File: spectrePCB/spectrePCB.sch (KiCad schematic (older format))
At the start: 23 parts, among them J1 USB_C_Receptacle, SW1 SW_Push, U1 Opamp_Dual_Generic, U2 ADG633YRU, U3 ATmega32U4-AU, U4 ADG633YRU, Y1 16MHz

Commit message: added footprints to components
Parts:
- C1, C2, C3, C4, C5, C6, C7: footprint (none) -> Capacitor_SMD:C_0603_1608Metric
- D1: footprint (none) -> LED_SMD:LED_0603_1608Metric
- F1: footprint (none) -> Fuse:Fuse_0603_1608Metric
- J1: footprint (none) -> Connector_USB:USB_C_Receptacle_Amphenol_12401548E4-2A
- R1, R2, R3, R4, R5, R6, R7: footprint (none) -> Resistor_SMD:R_0201_0603Metric
- SW1: footprint (none) -> Button_Switch_SMD:SW_SPST_TL3305A
- U1: footprint (none) -> Package_SO:SOIC-8_3.9x4.9mm_P1.27mm
- Y1: footprint (none) -> Crystal:Crystal_SMD_3225-4Pin_3.2x2.5mm
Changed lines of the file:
@@
 F 0 "R7" V 7150 4600 50  0000 C CNN
 F 1 "10k" V 7300 4600 50  0000 C CNN
-F 2 "" H 7250 4600 50  0001 C CNN
+F 2 "Resistor_SMD:R_0201_0603Metric" H 7250 4600 50  0001 C CNN
 F 3 "~" H 7250 4600 50  0001 C CNN
 	1    7250 4600
@@
 F 0 "R2" V 4495 3500 50  0000 C CNN
 F 1 "22" V 4586 3500 50  0000 C CNN
-F 2 "" H 4700 3500 50  0001 C CNN
+F 2 "Resistor_SMD:R_0201_0603Metric" H 4700 3500 50  0001 C CNN
 F 3 "~" H 4700 3500 50  0001 C CNN
 	1    4700 3500
@@
 F 0 "R4" V 4550 3600 50  0000 C CNN
 F 1 "22" V 4650 3600 50  0000 C CNN
-F 2 "" H 4450 3600 50  0001 C CNN
+F 2 "Resistor_SMD:R_0201_0603Metric" H 4450 3600 50  0001 C CNN
 F 3 "~" H 4450 3600 50  0001 C CNN
 	1    4450 3600
@@
 F 0 "C7" H 4842 4096 50  0000 L CNN
 F 1 "1uF" H 4842 4005 50  0000 L CNN
-F 2 "" H 4750 4050 50  0001 C CNN
+F 2 "Capacitor_SMD:C_0603_1608Metric" H 4750 4050 50  0001 C CNN
 F 3 "~" H 4750 4050 50  0001 C CNN
 	1    4750 4050
@@
 F 0 "C2" H 2142 1846 50  0000 L CNN
 F 1 "0.1uF" H 2142 1755 50  0000 L CNN
-F 2 "" H 2050 1800 50  0001 C CNN
+F 2 "Capacitor_SMD:C_0603_1608Metric" H 2050 1800 50  0001 C CNN
 F 3 "~" H 2050 1800 50  0001 C CNN
 	1    2050 1800
@@
 F 0 "C1" H 1742 1846 50  0000 L CNN
 F 1 "0.1uF" H 1742 1755 50  0000 L CNN
-F 2 "" H 1650 1800 50  0001 C CNN
+F 2 "Capacitor_SMD:C_0603_1608Metric" H 1650 1800 50  0001 C CNN
 F 3 "~" H 1650 1800 50  0001 C CNN
 	1    1650 1800
@@
 F 0 "C3" H 2542 1846 50  0000 L CNN
 F 1 "0.1uF" H 2542 1755 50  0000 L CNN
-F 2 "" H 2450 1800 50  0001 C CNN
+F 2 "Capacitor_SMD:C_0603_1608Metric" H 2450 1800 50  0001 C CNN
 F 3 "~" H 2450 1800 50  0001 C CNN
 	1    2450 1800
@@
 F 0 "C4" H 2892 1846 50  0000 L CNN
 F 1 "10uF" H 2892 1755 50  0000 L CNN
-F 2 "" H 2800 1800 50  0001 C CNN
+F 2 "Capacitor_SMD:C_0603_1608Metric" H 2800 1800 50  0001 C CNN
 F 3 "~" H 2800 1800 50  0001 C CNN
 	1    2800 1800
@@
 F 0 "C6" V 4500 2900 50  0000 C CNN
 F 1 "22pF" V 4600 2900 50  0000 C CNN
-F 2 "" H 4400 2900 50  0001 C CNN
+F 2 "Capacitor_SMD:C_0603_1608Metric" H 4400 2900 50  0001 C CNN
 F 3 "~" H 4400 2900 50  0001 C CNN
 	1    4400 2900
@@
 F 0 "C5" V 4200 2700 50  0000 C CNN
 F 1 "22pF" V 4300 2700 50  0000 C CNN
-F 2 "" H 4400 2700 50  0001 C CNN
+F 2 "Capacitor_SMD:C_0603_1608Metric" H 4400 2700 50  0001 C CNN
 F 3 "~" H 4400 2700 50  0001 C CNN
 	1    4400 2700
@@
 F 0 "Y1" V 4654 2944 50  0000 L CNN
 F 1 "16MHz" V 4745 2944 50  0000 L CNN
-F 2 "" H 4700 2800 50  0001 C CNN
+F 2 "Crystal:Crystal_SMD_3225-4Pin_3.2x2.5mm" H 4700 2800 50  0001 C CNN
 F 3 "~" H 4700 2800 50  0001 C CNN
 	1    4700 2800
@@
 F 0 "SW1" H 5000 2700 50  0000 C CNN
 F 1 "SW_Push" H 5000 2694 50  0001 C CNN
-F 2 "" H 5000 2700 50  0001 C CNN
+F 2 "Button_Switch_SMD:SW_SPST_TL3305A" H 5000 2700 50  0001 C CNN
 F 3 "~" H 5000 2700 50  0001 C CNN
 	1    5000 2500
@@
 F 0 "R1" H 5318 2146 50  0000 L CNN
 F 1 "10k" H 5318 2055 50  0000 L CNN
-F 2 "" H 5250 2100 50  0001 C CNN
+F 2 "Resistor_SMD:R_0201_0603Metric" H 5250 2100 50  0001 C CNN
 F 3 "~" H 5250 2100 50  0001 C CNN
 	1    5250 2100
@@
 F 0 "R6" H 2750 4200 50  0000 C CNN
 F 1 "5k" H 2750 4300 50  0000 C CNN
-F 2 "" H 2900 4250 50  0001 C CNN
+F 2 "Resistor_SMD:R_0201_0603Metric" H 2900 4250 50  0001 C CNN
 F 3 "~" H 2900 4250 50  0001 C CNN
 	1    2900 4250
@@
 F 0 "R5" H 2800 4200 50  0000 R CNN
 F 1 "5k" H 2800 4300 50  0000 R CNN
-F 2 "" H 2650 4250 50  0001 C CNN
+F 2 "Resistor_SMD:R_0201_0603Metric" H 2650 4250 50  0001 C CNN
 F 3 "~" H 2650 4250 50  0001 C CNN
 	1    2650 4250
@@
 F 0 "F1" V 2100 3000 50  0000 C CNN
 F 1 "500mA" V 2200 3000 50  0000 C CNN
-F 2 "" H 2200 2800 50  0001 L CNN
+F 2 "Fuse:Fuse_0603_1608Metric" H 2200 2800 50  0001 L CNN
 F 3 "~" H 2150 3000 50  0001 C CNN
 	1    2150 3000
@@
 F 0 "J1" H 1357 6067 50  0000 C CNN
 F 1 "USB_C_Receptacle" H 1357 5976 50  0000 C CNN
-F 2 "" H 1400 4800 50  0001 C CNN
+F 2 "Connector_USB:USB_C_Receptacle_Amphenol_12401548E4-2A" H 1400 4800 50  0001 C CNN
 F 3 "https://www.usb.org/sites/default/files/documents/usb_type-c.zip" H 1400 4800 50  0001 C CNN
 	1    1250 4800
@@
 F 0 "D1" H 2900 3450 50  0000 C CNN
 F 1 "LED_Red" H 2900 3434 50  0001 C CNN
-F 2 "" V 2900 3550 50  0001 C CNN
+F 2 "LED_SMD:LED_0603_1608Metric" V 2900 3550 50  0001 C CNN
 F 3 "~" V 2900 3550 50  0001 C CNN
 	1    2900 3550
@@
 F 0 "R3" V 2995 3550 50  0000 C CNN
 F 1 "1k" V 3086 3550 50  0000 C CNN
-F 2 "" H 3200 3550 50  0001 C CNN
+F 2 "Resistor_SMD:R_0201_0603Metric" H 3200 3550 50  0001 C CNN
 F 3 "~" H 3200 3550 50  0001 C CNN
 	1    3200 3550
@@
 F 0 "U1" H 9650 1617 50  0000 C CNN
 F 1 "Opamp_Dual_Generic" H 9650 1526 50  0000 C CNN
-F 2 "" H 9650 1250 50  0001 C CNN
+F 2 "Package_SO:SOIC-8_3.9x4.9mm_P1.27mm" H 9650 1250 50  0001 C CNN
 F 3 "~" H 9650 1250 50  0001 C CNN
 	1    9650 1250
@@
 F 0 "U1" H 8550 1300 50  0000 L CNN
 F 1 "Opamp_Dual_Generic" H 7950 1200 50  0000 L CNN
-F 2 "" H 8900 1250 50  0001 C CNN
+F 2 "Package_SO:SOIC-8_3.9x4.9mm_P1.27mm" H 8900 1250 50  0001 C CNN
 F 3 "~" H 8900 1250 50  0001 C CNN
 	3    8900 1250

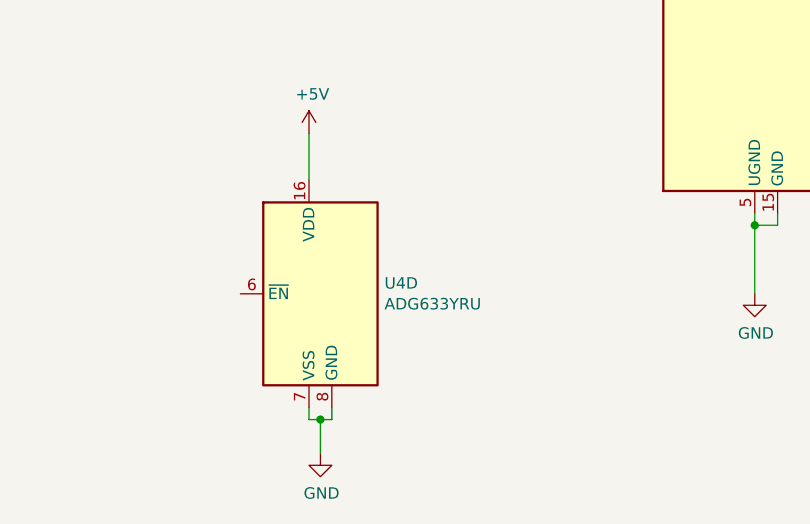
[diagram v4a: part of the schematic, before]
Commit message: placed resistors, added edges, fixing GND net
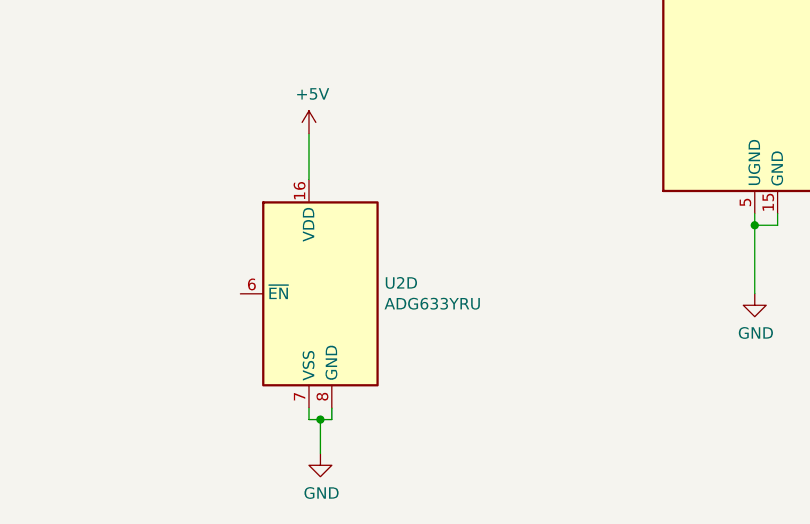
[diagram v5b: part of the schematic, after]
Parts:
- R1, R2, R3, R4, R5, R6, R7: footprint Resistor_SMD:R_0201_0603Metric -> Resistor_SMD:R_0603_1608Metric
- renumbered U4 to U2
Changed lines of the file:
@@
 F 0 "R7" V 7150 4600 50  0000 C CNN
 F 1 "10k" V 7300 4600 50  0000 C CNN
-F 2 "Resistor_SMD:R_0201_0603Metric" H 7250 4600 50  0001 C CNN
+F 2 "Resistor_SMD:R_0603_1608Metric" H 7250 4600 50  0001 C CNN
 F 3 "~" H 7250 4600 50  0001 C CNN
 	1    7250 4600
@@
 F 0 "R2" V 4495 3500 50  0000 C CNN
 F 1 "22" V 4586 3500 50  0000 C CNN
-F 2 "Resistor_SMD:R_0201_0603Metric" H 4700 3500 50  0001 C CNN
+F 2 "Resistor_SMD:R_0603_1608Metric" H 4700 3500 50  0001 C CNN
 F 3 "~" H 4700 3500 50  0001 C CNN
 	1    4700 3500
@@
 F 0 "R4" V 4550 3600 50  0000 C CNN
 F 1 "22" V 4650 3600 50  0000 C CNN
-F 2 "Resistor_SMD:R_0201_0603Metric" H 4450 3600 50  0001 C CNN
+F 2 "Resistor_SMD:R_0603_1608Metric" H 4450 3600 50  0001 C CNN
 F 3 "~" H 4450 3600 50  0001 C CNN
 	1    4450 3600
@@
 F 0 "R1" H 5318 2146 50  0000 L CNN
 F 1 "10k" H 5318 2055 50  0000 L CNN
-F 2 "Resistor_SMD:R_0201_0603Metric" H 5250 2100 50  0001 C CNN
+F 2 "Resistor_SMD:R_0603_1608Metric" H 5250 2100 50  0001 C CNN
 F 3 "~" H 5250 2100 50  0001 C CNN
 	1    5250 2100
@@
 F 0 "R6" H 2750 4200 50  0000 C CNN
 F 1 "5k" H 2750 4300 50  0000 C CNN
-F 2 "Resistor_SMD:R_0201_0603Metric" H 2900 4250 50  0001 C CNN
+F 2 "Resistor_SMD:R_0603_1608Metric" H 2900 4250 50  0001 C CNN
 F 3 "~" H 2900 4250 50  0001 C CNN
 	1    2900 4250
@@
 F 0 "R5" H 2800 4200 50  0000 R CNN
 F 1 "5k" H 2800 4300 50  0000 R CNN
-F 2 "Resistor_SMD:R_0201_0603Metric" H 2650 4250 50  0001 C CNN
+F 2 "Resistor_SMD:R_0603_1608Metric" H 2650 4250 50  0001 C CNN
 F 3 "~" H 2650 4250 50  0001 C CNN
 	1    2650 4250
@@
 F 0 "R3" V 2995 3550 50  0000 C CNN
 F 1 "1k" V 3086 3550 50  0000 C CNN
-F 2 "Resistor_SMD:R_0201_0603Metric" H 3200 3550 50  0001 C CNN
+F 2 "Resistor_SMD:R_0603_1608Metric" H 3200 3550 50  0001 C CNN
 F 3 "~" H 3200 3550 50  0001 C CNN
 	1    3200 3550
@@
 P 3850 6150
 AR Path="/6055A05F/60CB5E9C" Ref="U?"  Part="4"
-AR Path="/60CB5E9C" Ref="U4"  Part="4"
-F 0 "U4" H 4180 6196 50  0000 L CNN
+AR Path="/60CB5E9C" Ref="U2"  Part="4"
+F 0 "U2" H 4180 6196 50  0000 L CNN
 F 1 "ADG633YRU" H 4180 6105 50  0000 L CNN
 F 2 "Package_SO:TSSOP-20_4.4x6.5mm_P0.65mm" H 3850 6150 50  0001 C CNN

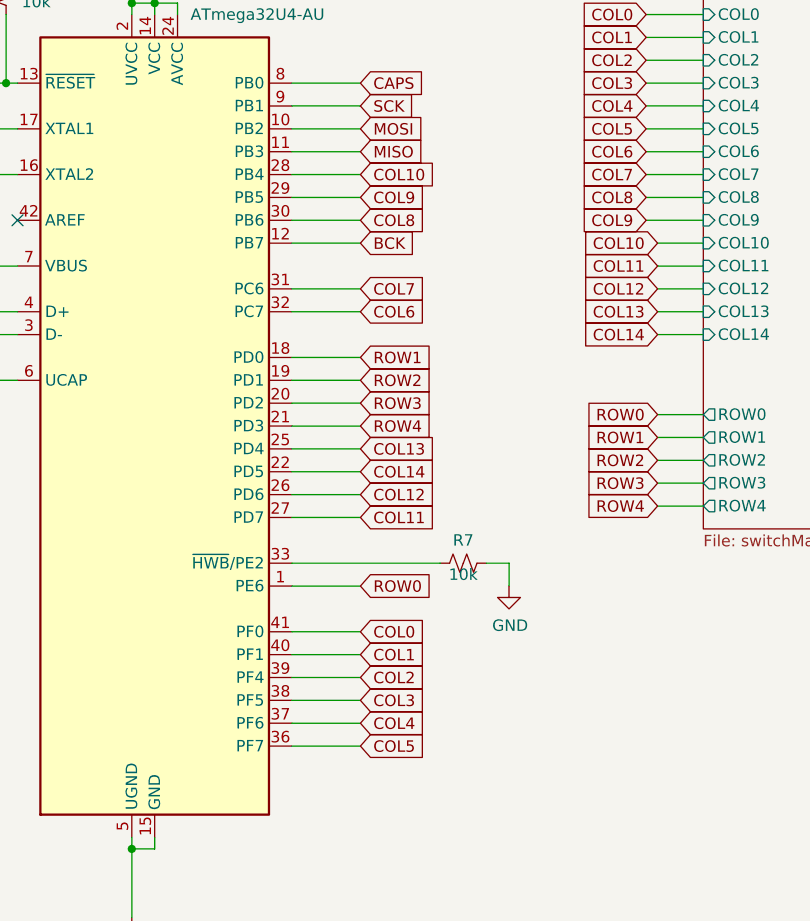
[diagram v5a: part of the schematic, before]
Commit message: finished routing pcb
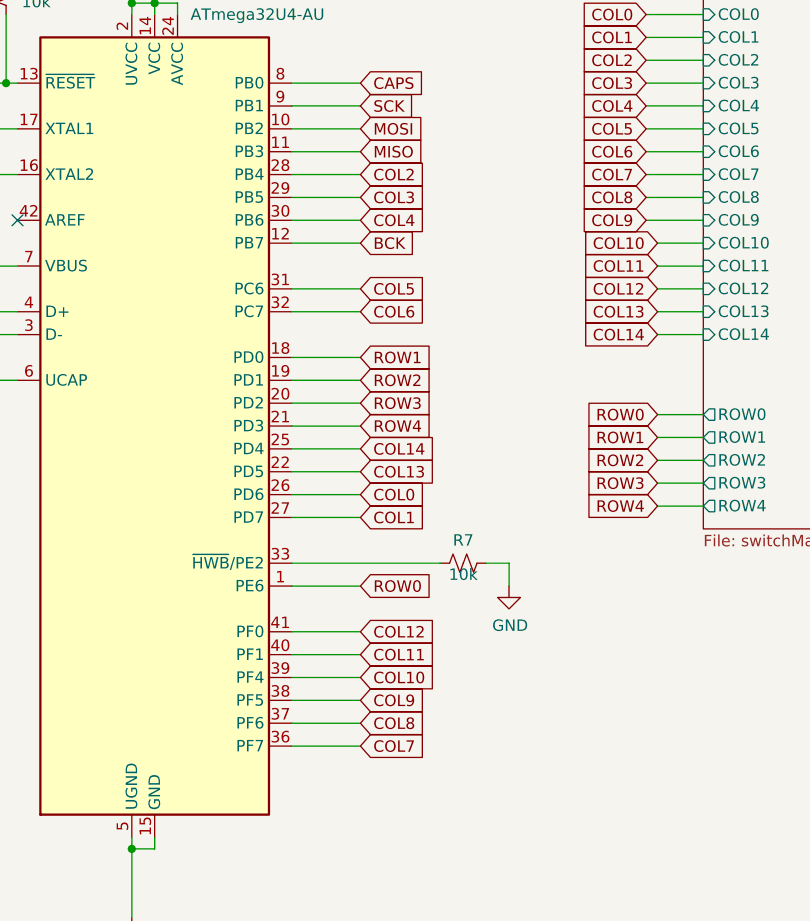
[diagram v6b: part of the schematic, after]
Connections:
- net COL0: now also U3.26 (PD6); no longer U3.41 (PF0)
- net COL1: now also U3.27 (PD7); no longer U3.40 (PF1)
- net COL10: now also U3.39 (PF4); no longer U3.28 (PB4)
- net COL11: now also U3.40 (PF1); no longer U3.27 (PD7)
- net COL12: now also U3.41 (PF0); no longer U3.26 (PD6)
- net COL13: now also U3.22 (PD5); no longer U3.25 (PD4)
- net COL14: now also U3.25 (PD4); no longer U3.22 (PD5)
- net COL2: now also U3.28 (PB4); no longer U3.39 (PF4)
- net COL3: now also U3.29 (PB5); no longer U3.38 (PF5)
- net COL4: now also U3.30 (PB6); no longer U3.37 (PF6)
- net COL5: now also U3.31 (PC6); no longer U3.36 (PF7)
- net COL7: now also U3.36 (PF7); no longer U3.31 (PC6)
- net COL8: now also U3.37 (PF6); no longer U3.30 (PB6)
- net COL9: now also U3.38 (PF5); no longer U3.29 (PB5)
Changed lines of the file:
@@
 Wire Wire Line
 	10000 4350 10000 4600
-Text GLabel 6800 4900 2    50   Input ~ 0
-COL0
-Text GLabel 6800 5000 2    50   Input ~ 0
-COL1
-Text GLabel 6800 5100 2    50   Input ~ 0
-COL2
-Text GLabel 6800 5200 2    50   Input ~ 0
-COL3
-Text GLabel 6800 5300 2    50   Input ~ 0
-COL4
-Text GLabel 6800 5400 2    50   Input ~ 0
-COL5
-Text GLabel 6800 3500 2    50   Input ~ 0
-COL6
-Text GLabel 6800 3400 2    50   Input ~ 0
-COL7
-Text GLabel 6800 3100 2    50   Input ~ 0
-COL8
-Text GLabel 6800 3000 2    50   Input ~ 0
-COL9
-Text GLabel 6800 2900 2    50   Input ~ 0
-COL10
-Text GLabel 6800 4400 2    50   Input ~ 0
-COL11
-Text GLabel 6800 4300 2    50   Input ~ 0
-COL12
-Text GLabel 6800 4100 2    50   Input ~ 0
-COL13
-Text GLabel 6800 4200 2    50   Input ~ 0
-COL14
 Text GLabel 6800 4700 2    50   Input ~ 0
 ROW0
@@
 	1    0    0    -1
 $EndComp
+Text GLabel 6800 4400 2    50   Input ~ 0
+COL1
+Text GLabel 6800 4300 2    50   Input ~ 0
+COL0
+Text GLabel 6800 2900 2    50   Input ~ 0
+COL2
+Text GLabel 6800 3000 2    50   Input ~ 0
+COL3
+Text GLabel 6800 3100 2    50   Input ~ 0
+COL4
+Text GLabel 6800 3400 2    50   Input ~ 0
+COL5
+Text GLabel 6800 3500 2    50   Input ~ 0
+COL6
+Text GLabel 6800 5400 2    50   Input ~ 0
+COL7
+Text GLabel 6800 5300 2    50   Input ~ 0
+COL8
+Text GLabel 6800 5200 2    50   Input ~ 0
+COL9
+Text GLabel 6800 5100 2    50   Input ~ 0
+COL10
+Text GLabel 6800 5000 2    50   Input ~ 0
+COL11
+Text GLabel 6800 4200 2    50   Input ~ 0
+COL13
+Text GLabel 6800 4100 2    50   Input ~ 0
+COL14
+Text GLabel 6800 4900 2    50   Input ~ 0
+COL12
 $EndSCHEMATC
